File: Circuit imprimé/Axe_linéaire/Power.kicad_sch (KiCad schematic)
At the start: 0 parts

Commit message: Ajout des protections sur l'alimentation
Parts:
- added C?: C_Polarized, symbol Device:C_Polarized
- added C?: C, symbol Device:C
- added D?: D_Zener, symbol Device:D_Zener
- added FB?: FerriteBead, symbol Device:FerriteBead
- added Q?: LP2301LT1G, Package_TO_SOT_SMD:SOT-23, symbol Transistor_FET:VP0610T
- added R?: 1k, symbol Device:R
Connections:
- new net: C?.1, D?.1 (K), FB?.2, Q?.2 (S)
- new net: D?.2 (A), Q?.1 (G), R?.1
- new net +VDC: Q?.3 (D)
- new net GND: C?.2, C?.2, R?.2
- new net VDC: C?.1, FB?.1
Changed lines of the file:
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@@
 (kicad_sch (version 20211123) (generator eeschema)
   (paper "A4")
+  (junction (at 52.07 30.48) (diameter 0) (color 0 0 0 0)
+  )
+  (junction (at 59.69 30.48) (diameter 0) (color 0 0 0 0)
+  )
+  (junction (at 41.91 38.1) (diameter 0) (color 0 0 0 0)
+  )
+  (junction (at 41.91 30.48) (diameter 0) (color 0 0 0 0)
+  )
+  (junction (at 41.91 22.86) (diameter 0) (color 0 0 0 0)
+  )
+  (junction (at 52.07 22.86) (diameter 0) (color 0 0 0 0)
+  )
+  (junction (at 59.69 22.86) (diameter 0) (color 0 0 0 0)
+  )
+  (wire (pts (xy 36.83 36.83) (xy 36.83 38.1))
+    (stroke (width 0) (type default) (color 0 0 0 0))
+  )
+  (wire (pts (xy 52.07 30.48) (xy 52.07 38.1))
+    (stroke (width 0) (type default) (color 0 0 0 0))
+  )
+  (wire (pts (xy 59.69 22.86) (xy 66.04 22.86))
+    (stroke (width 0) (type default) (color 0 0 0 0))
+  )
+  (wire (pts (xy 36.83 38.1) (xy 41.91 38.1))
+    (stroke (width 0) (type default) (color 0 0 0 0))
+  )
+  (wire (pts (xy 31.75 36.83) (xy 36.83 36.83))
+    (stroke (width 0) (type default) (color 0 0 0 0))
+  )
+  (wire (pts (xy 41.91 22.86) (xy 52.07 22.86))
+    (stroke (width 0) (type default) (color 0 0 0 0))
+  )
+  (wire (pts (xy 41.91 38.1) (xy 52.07 38.1))
+    (stroke (width 0) (type default) (color 0 0 0 0))
+  )
+  (wire (pts (xy 36.83 30.48) (xy 41.91 30.48))
+    (stroke (width 0) (type default) (color 0 0 0 0))
+  )
+  (wire (pts (xy 52.07 30.48) (xy 59.69 30.48))
+    (stroke (width 0) (type default) (color 0 0 0 0))
+  )
+  (wire (pts (xy 59.69 30.48) (xy 66.04 30.48))
+    (stroke (width 0) (type default) (color 0 0 0 0))
+  )
+  (symbol (lib_id "Device:C_Polarized") (at 52.07 26.67 0) (unit 1)
+    (in_bom yes) (on_board yes) (fields_autoplaced)
+    (property "Reference" "C?" (id 0) (at 55.88 24.5109 0)
+      (effects (font (size 1.27 1.27)) (justify left))
+    )
+    (property "Value" "C_Polarized" (id 1) (at 55.88 27.0509 0)
+      (effects (font (size 1.27 1.27)) (justify left))
+    )
+    (property "Footprint" "" (id 2) (at 53.0352 30.48 0)
+      (effects (font (size 1.27 1.27)) hide)
+    )
+    (property "Datasheet" "~" (id 3) (at 52.07 26.67 0)
+      (effects (font (size 1.27 1.27)) hide)
+    )
+    (pin "1")
+    (pin "2")
+  )
+  (symbol (lib_id "Device:FerriteBead") (at 55.88 22.86 270) (unit 1)
+    (in_bom yes) (on_board yes) (fields_autoplaced)
+    (property "Reference" "FB?" (id 0) (at 55.9308 15.24 90))
+    (property "Value" "FerriteBead" (id 1) (at 55.9308 17.78 90))
+    (property "Footprint" "" (id 2) (at 55.88 21.082 90)
+      (effects (font (size 1.27 1.27)) hide)
+    )
+    (property "Datasheet" "~" (id 3) (at 55.88 22.86 0)
+      (effects (font (size 1.27 1.27)) hide)
+    )
+    (pin "1")
+    (pin "2")
+  )
+  (symbol (lib_id "Device:D_Zener") (at 41.91 26.67 270) (unit 1)
+    (in_bom yes) (on_board yes) (fields_autoplaced)
+    (property "Reference" "D?" (id 0) (at 44.45 25.3999 90)
+      (effects (font (size 1.27 1.27)) (justify left))
+    )
+    (property "Value" "D_Zener" (id 1) (at 44.45 27.9399 90)
+      (effects (font (size 1.27 1.27)) (justify left))
+    )
+    (property "Footprint" "" (id 2) (at 41.91 26.67 0)
+      (effects (font (size 1.27 1.27)) hide)
+    )
+    (property "Datasheet" "~" (id 3) (at 41.91 26.67 0)
+      (effects (font (size 1.27 1.27)) hide)
+    )
+    (pin "1")
+    (pin "2")
+  )
+  (symbol (lib_id "power:+VDC") (at 31.75 22.86 0) (unit 1)
+    (in_bom yes) (on_board yes) (fields_autoplaced)
+    (property "Reference" "#PWR?" (id 0) (at 31.75 25.4 0)
+      (effects (font (size 1.27 1.27)) hide)
+    )
+    (property "Value" "+VDC" (id 1) (at 31.75 15.24 0))
+    (property "Footprint" "" (id 2) (at 31.75 22.86 0)
+      (effects (font (size 1.27 1.27)) hide)
+    )
+    (property "Datasheet" "" (id 3) (at 31.75 22.86 0)
+      (effects (font (size 1.27 1.27)) hide)
+    )
+    (pin "1")
+  )
+  (symbol (lib_id "power:GND") (at 66.04 30.48 0) (unit 1)
+    (in_bom yes) (on_board yes) (fields_autoplaced)
+    (property "Reference" "#PWR?" (id 0) (at 66.04 36.83 0)
+      (effects (font (size 1.27 1.27)) hide)
+    )
+    (property "Value" "GND" (id 1) (at 66.04 35.56 0))
+    (property "Footprint" "" (id 2) (at 66.04 30.48 0)
+      (effects (font (size 1.27 1.27)) hide)
+    )
+    (property "Datasheet" "" (id 3) (at 66.04 30.48 0)
+      (effects (font (size 1.27 1.27)) hide)
+    )
+    (pin "1")
+  )
+  (symbol (lib_id "power:VDC") (at 66.04 22.86 0) (unit 1)
+    (in_bom yes) (on_board yes) (fields_autoplaced)
+    (property "Reference" "#PWR?" (id 0) (at 66.04 25.4 0)
+      (effects (font (size 1.27 1.27)) hide)
+    )
+    (property "Value" "VDC" (id 1) (at 66.04 17.78 0))
+    (property "Footprint" "" (id 2) (at 66.04 22.86 0)
+      (effects (font (size 1.27 1.27)) hide)
+    )
+    (property "Datasheet" "" (id 3) (at 66.04 22.86 0)
+      (effects (font (size 1.27 1.27)) hide)
+    )
+    (pin "1")
+  )
+  (symbol (lib_id "Device:C") (at 59.69 26.67 0) (unit 1)
+    (in_bom yes) (on_board yes) (fields_autoplaced)
+    (property "Reference" "C?" (id 0) (at 63.5 25.3999 0)
+      (effects (font (size 1.27 1.27)) (justify left))
+    )
+    (property "Value" "C" (id 1) (at 63.5 27.9399 0)
+      (effects (font (size 1.27 1.27)) (justify left))
+    )
+    (property "Footprint" "" (id 2) (at 60.6552 30.48 0)
+      (effects (font (size 1.27 1.27)) hide)
+    )
+    (property "Datasheet" "~" (id 3) (at 59.69 26.67 0)
+      (effects (font (size 1.27 1.27)) hide)
+    )
+    (pin "1")
+    (pin "2")
+  )
+  (symbol (lib_id "Transistor_FET:VP0610T") (at 36.83 25.4 90) (unit 1)
+    (in_bom yes) (on_board yes)
+    (property "Reference" "Q?" (id 0) (at 36.83 15.24 90))
+    (property "Value" "LP2301LT1G" (id 1) (at 40.64 17.78 90))
+    (property "Footprint" "Package_TO_SOT_SMD:SOT-23" (id 2) (at 38.735 20.32 0)
+      (effects (font (size 1.27 1.27) italic) (justify left) hide)
+    )
+    (property "Datasheet" "https://datasheet.lcsc.com/lcsc/1810251911_LRC-LP2301LT1G_C77937.pdf" (id 3) (at 36.83 25.4 0)
+      (effects (font (size 1.27 1.27)) (justify left) hide)
+    )
+    (pin "1")
+    (pin "2")
+    (pin "3")
+  )
+  (symbol (lib_id "Device:R") (at 41.91 34.29 0) (unit 1)
+    (in_bom yes) (on_board yes) (fields_autoplaced)
+    (property "Reference" "R?" (id 0) (at 44.45 33.0199 0)
+      (effects (font (size 1.27 1.27)) (justify left))
+    )
+    (property "Value" "1k" (id 1) (at 44.45 35.5599 0)
+      (effects (font (size 1.27 1.27)) (justify left))
+    )
+    (property "Footprint" "" (id 2) (at 40.132 34.29 90)
+      (effects (font (size 1.27 1.27)) hide)
+    )
+    (property "Datasheet" "~" (id 3) (at 41.91 34.29 0)
+      (effects (font (size 1.27 1.27)) hide)
+    )
+    (pin "1")
+    (pin "2")
+  )
+  (symbol (lib_id "power:GND") (at 31.75 36.83 0) (unit 1)
+    (in_bom yes) (on_board yes) (fields_autoplaced)
+    (property "Reference" "#PWR?" (id 0) (at 31.75 43.18 0)
+      (effects (font (size 1.27 1.27)) hide)
+    )
+    (property "Value" "GND" (id 1) (at 31.75 41.91 0))
+    (property "Footprint" "" (id 2) (at 31.75 36.83 0)
+      (effects (font (size 1.27 1.27)) hide)
+    )
+    (property "Datasheet" "" (id 3) (at 31.75 36.83 0)
+      (effects (font (size 1.27 1.27)) hide)
+    )
+    (pin "1")
+  )
 )

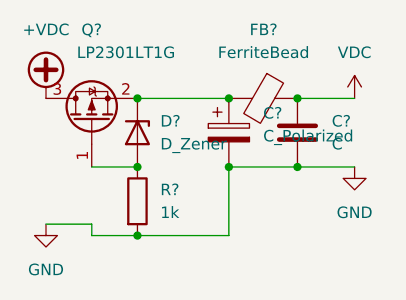
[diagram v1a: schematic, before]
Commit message: Ajout de l'IMU + modèle du photointerrupteur
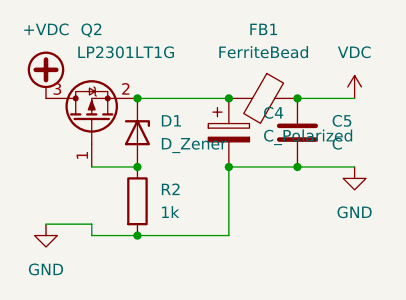
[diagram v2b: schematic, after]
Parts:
- gave numbers to parts that had none: 6
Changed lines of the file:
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@@
   (symbol (lib_id "Device:C_Polarized") (at 52.07 26.67 0) (unit 1)
     (in_bom yes) (on_board yes) (fields_autoplaced)
-    (property "Reference" "C?" (id 0) (at 55.88 24.5109 0)
+    (property "Reference" "C4" (id 0) (at 55.88 24.5109 0)
       (effects (font (size 1.27 1.27)) (justify left))
     )
@@
   (symbol (lib_id "Device:FerriteBead") (at 55.88 22.86 270) (unit 1)
     (in_bom yes) (on_board yes) (fields_autoplaced)
-    (property "Reference" "FB?" (id 0) (at 55.9308 15.24 90))
+    (property "Reference" "FB1" (id 0) (at 55.9308 15.24 90))
     (property "Value" "FerriteBead" (id 1) (at 55.9308 17.78 90))
     (property "Footprint" "" (id 2) (at 55.88 21.082 90)
@@
   (symbol (lib_id "Device:D_Zener") (at 41.91 26.67 270) (unit 1)
     (in_bom yes) (on_board yes) (fields_autoplaced)
-    (property "Reference" "D?" (id 0) (at 44.45 25.3999 90)
+    (property "Reference" "D1" (id 0) (at 44.45 25.3999 90)
       (effects (font (size 1.27 1.27)) (justify left))
     )
@@
   (symbol (lib_id "power:+VDC") (at 31.75 22.86 0) (unit 1)
     (in_bom yes) (on_board yes) (fields_autoplaced)
-    (property "Reference" "#PWR?" (id 0) (at 31.75 25.4 0)
+    (property "Reference" "#PWR026" (id 0) (at 31.75 25.4 0)
       (effects (font (size 1.27 1.27)) hide)
     )
@@
   (symbol (lib_id "power:GND") (at 66.04 30.48 0) (unit 1)
     (in_bom yes) (on_board yes) (fields_autoplaced)
-    (property "Reference" "#PWR?" (id 0) (at 66.04 36.83 0)
+    (property "Reference" "#PWR029" (id 0) (at 66.04 36.83 0)
       (effects (font (size 1.27 1.27)) hide)
     )
@@
   (symbol (lib_id "power:VDC") (at 66.04 22.86 0) (unit 1)
     (in_bom yes) (on_board yes) (fields_autoplaced)
-    (property "Reference" "#PWR?" (id 0) (at 66.04 25.4 0)
+    (property "Reference" "#PWR028" (id 0) (at 66.04 25.4 0)
       (effects (font (size 1.27 1.27)) hide)
     )
@@
   (symbol (lib_id "Device:C") (at 59.69 26.67 0) (unit 1)
     (in_bom yes) (on_board yes) (fields_autoplaced)
-    (property "Reference" "C?" (id 0) (at 63.5 25.3999 0)
+    (property "Reference" "C5" (id 0) (at 63.5 25.3999 0)
       (effects (font (size 1.27 1.27)) (justify left))
     )
@@
   (symbol (lib_id "Transistor_FET:VP0610T") (at 36.83 25.4 90) (unit 1)
     (in_bom yes) (on_board yes)
-    (property "Reference" "Q?" (id 0) (at 36.83 15.24 90))
+    (property "Reference" "Q2" (id 0) (at 36.83 15.24 90))
     (property "Value" "LP2301LT1G" (id 1) (at 40.64 17.78 90))
     (property "Footprint" "Package_TO_SOT_SMD:SOT-23" (id 2) (at 38.735 20.32 0)
@@
   (symbol (lib_id "Device:R") (at 41.91 34.29 0) (unit 1)
     (in_bom yes) (on_board yes) (fields_autoplaced)
-    (property "Reference" "R?" (id 0) (at 44.45 33.0199 0)
+    (property "Reference" "R2" (id 0) (at 44.45 33.0199 0)
       (effects (font (size 1.27 1.27)) (justify left))
     )
@@
   (symbol (lib_id "power:GND") (at 31.75 36.83 0) (unit 1)
     (in_bom yes) (on_board yes) (fields_autoplaced)
-    (property "Reference" "#PWR?" (id 0) (at 31.75 43.18 0)
+    (property "Reference" "#PWR027" (id 0) (at 31.75 43.18 0)
       (effects (font (size 1.27 1.27)) hide)
     )

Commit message: circuit V1
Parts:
- C4: value C_Polarized -> 10u; footprint (none) -> Capacitor_SMD:CP_Elec_6.3x7.7
- C5: value C -> 100n; footprint (none) -> Library:Cap 100nf 0805
- D1: footprint (none) -> Library:SOD223
- FB1: footprint (none) -> Library:ferrite Bead
- R2: footprint (none) -> Resistor_SMD:R_0603_1608Metric
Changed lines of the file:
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@@
+    (stroke (width 0) (type default) (color 0 0 0 0))
+  )
+  (wire (pts (xy 66.04 20.32) (xy 66.04 22.86))
     (stroke (width 0) (type default) (color 0 0 0 0))
   )
@@
       (effects (font (size 1.27 1.27)) (justify left))
     )
-    (property "Value" "C_Polarized" (id 1) (at 55.88 27.0509 0)
+    (property "Value" "10u" (id 1) (at 55.88 27.0509 0)
       (effects (font (size 1.27 1.27)) (justify left))
     )
-    (property "Footprint" "" (id 2) (at 53.0352 30.48 0)
+    (property "Footprint" "Capacitor_SMD:CP_Elec_6.3x7.7" (id 2) (at 53.0352 30.48 0)
       (effects (font (size 1.27 1.27)) hide)
     )
@@
     (property "Reference" "FB1" (id 0) (at 55.9308 15.24 90))
     (property "Value" "FerriteBead" (id 1) (at 55.9308 17.78 90))
-    (property "Footprint" "" (id 2) (at 55.88 21.082 90)
+    (property "Footprint" "Library:ferrite Bead" (id 2) (at 55.88 21.082 90)
       (effects (font (size 1.27 1.27)) hide)
     )
@@
       (effects (font (size 1.27 1.27)) (justify left))
     )
-    (property "Footprint" "" (id 2) (at 41.91 26.67 0)
+    (property "Footprint" "Library:SOD223" (id 2) (at 41.91 26.67 0)
       (effects (font (size 1.27 1.27)) hide)
     )
@@
     (pin "1")
   )
-  (symbol (lib_id "power:VDC") (at 66.04 22.86 0) (unit 1)
-    (in_bom yes) (on_board yes) (fields_autoplaced)
-    (property "Reference" "#PWR028" (id 0) (at 66.04 25.4 0)
-      (effects (font (size 1.27 1.27)) hide)
-    )
-    (property "Value" "VDC" (id 1) (at 66.04 17.78 0))
-    (property "Footprint" "" (id 2) (at 66.04 22.86 0)
-      (effects (font (size 1.27 1.27)) hide)
-    )
-    (property "Datasheet" "" (id 3) (at 66.04 22.86 0)
-      (effects (font (size 1.27 1.27)) hide)
-    )
-    (pin "1")
-  )
   (symbol (lib_id "Device:C") (at 59.69 26.67 0) (unit 1)
     (in_bom yes) (on_board yes) (fields_autoplaced)
@@
       (effects (font (size 1.27 1.27)) (justify left))
     )
-    (property "Value" "C" (id 1) (at 63.5 27.9399 0)
+    (property "Value" "100n" (id 1) (at 63.5 27.9399 0)
       (effects (font (size 1.27 1.27)) (justify left))
     )
-    (property "Footprint" "" (id 2) (at 60.6552 30.48 0)
+    (property "Footprint" "Library:Cap 100nf 0805" (id 2) (at 60.6552 30.48 0)
       (effects (font (size 1.27 1.27)) hide)
     )
@@
     (pin "1")
     (pin "2")
+  )
+  (symbol (lib_id "power:VDC") (at 66.04 20.32 0) (unit 1)
+    (in_bom yes) (on_board yes) (fields_autoplaced)
+    (property "Reference" "#PWR0112" (id 0) (at 66.04 22.86 0)
+      (effects (font (size 1.27 1.27)) hide)
+    )
+    (property "Value" "VDC" (id 1) (at 66.04 15.24 0))
+    (property "Footprint" "" (id 2) (at 66.04 20.32 0)
+      (effects (font (size 1.27 1.27)) hide)
+    )
+    (property "Datasheet" "" (id 3) (at 66.04 20.32 0)
+      (effects (font (size 1.27 1.27)) hide)
+    )
+    (pin "1")
   )
   (symbol (lib_id "Transistor_FET:VP0610T") (at 36.83 25.4 90) (unit 1)
@@
       (effects (font (size 1.27 1.27)) (justify left))
     )
-    (property "Footprint" "" (id 2) (at 40.132 34.29 90)
+    (property "Footprint" "Resistor_SMD:R_0603_1608Metric" (id 2) (at 40.132 34.29 90)
       (effects (font (size 1.27 1.27)) hide)
     )
